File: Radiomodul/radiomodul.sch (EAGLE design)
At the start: 29 parts, among them IC1 MCP601R, Q1 12MHz, U1 LPC1343FBD48, U2 LM1117-3.3, U3 MCP130T

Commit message: the name corrected
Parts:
- removed D1: (no value), diode:DIODE-SMB
- removed D2: P6SMB18CA, Heinrich:SHOTKY-SMDSMB
- removed JP2: E31, microbuilder:HEADER-1X7ROUND
- removed R14, R16: 4k7, rcl:R-EU_R0805
- removed U3: MCP130T, microbuilder:MCP130TWAVE
- added C11, C12, C17: 100nF, rcl:C-EUC0805
- added C14: 100pF, rcl:C-EUC0805
- added C18: 10µF, Heinrich:CAP_TANTALUMSMCA
- added IC2: AD5243, Heinrich:AD5243
- added IC3: TXS0104, Heinrich:TXS0104
- added IC4: TXB0104PWR, Heinrich:TXB0104PWR
- added IC6: E910.15, Heinrich:E910.15
- added R5: 10, rcl:R-EU_R0805
- added R6: 10k, rcl:R-EU_R0805
- C7, C8: value 10uF -> 100nF; device rcl:CPOL-EUSMCC -> rcl:C-EUC0805
- U2: value LM1117-3.3 -> MCP130T; device microbuilder:LM1117SOT223-REFLOW -> microbuilder:MCP130TWAVE
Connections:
- removed net 12V: D1.A, JP2.1
- removed net G1: JP2.7
- removed net G2: JP2.6
- removed net G3: JP2.5
- removed net G4: JP2.4
- new net /SEN: IC4.A3, U1.PIO1_5/!RTS!/CT32B0_CAP0
- new net 5.0V: C10.1, C17.1, C18.+, C7.1, IC2.VDD, IC3.VCCB, IC4.VCCB, IC6.VCC
- new net IBUS: R5.2
- new net N$10: IC4.B3, IC6.SEN/STA
- new net N$7: IC4.B2, IC6.TXD
- new net N$9: C14.1, IC6.BUS, R5.1
- new net RING: IC3.A3, U1.PIO0_3/USB_VBUS
- new net RXD: IC4.A1, U1.PIO1_6/RXD/CT32B0_MAT0
- new net R_BASE: IC2.W2
- new net R_RING: IC3.B3
- new net R_TIP: IC2.A1
- new net TXD: IC4.A2, U1.PIO1_7/TXD/CT32B0_MAT1
- net /RESET: now also R6.1, U2.RST; no longer U3.RST
- net 3.3V: now also C11.1, C12.1, C8.1, IC3.OE, IC3.VCCA, IC4.OE, IC4.VCCA, R6.2, U2.VCC; no longer C10.1, C7.+, R14.2, R16.2, U2.OUT, U3.VCC
- net GND: now also C11.2, C12.2, C14.2, C17.2, C18.-, C7.2, C8.2, IC2.GND, IC3.GND, IC6.GND, U2.GND; no longer C7.-, C8.-, D2.A, JP2.2, U2.ADJ, U3.GND
- net LICHT: no longer JP2.3
- net N$1: now also IC2.SDA, IC3.B1; no longer C8.+, D1.C, D2.C, U2.IN
- net N$3: now also IC2.SCL, IC3.B2; no longer U1.PIO1_6/RXD/CT32B0_MAT0
- net N$5: now also IC4.B1, IC6.RXD; no longer U1.PIO1_7/TXD/CT32B0_MAT1
- net N$6: now also IC2.A2, IC2.W1; no longer U1.PIO1_5/!RTS!/CT32B0_CAP0
- net SCL: now also IC3.A2; no longer R16.1
- net SDA: now also IC3.A1; no longer R14.1

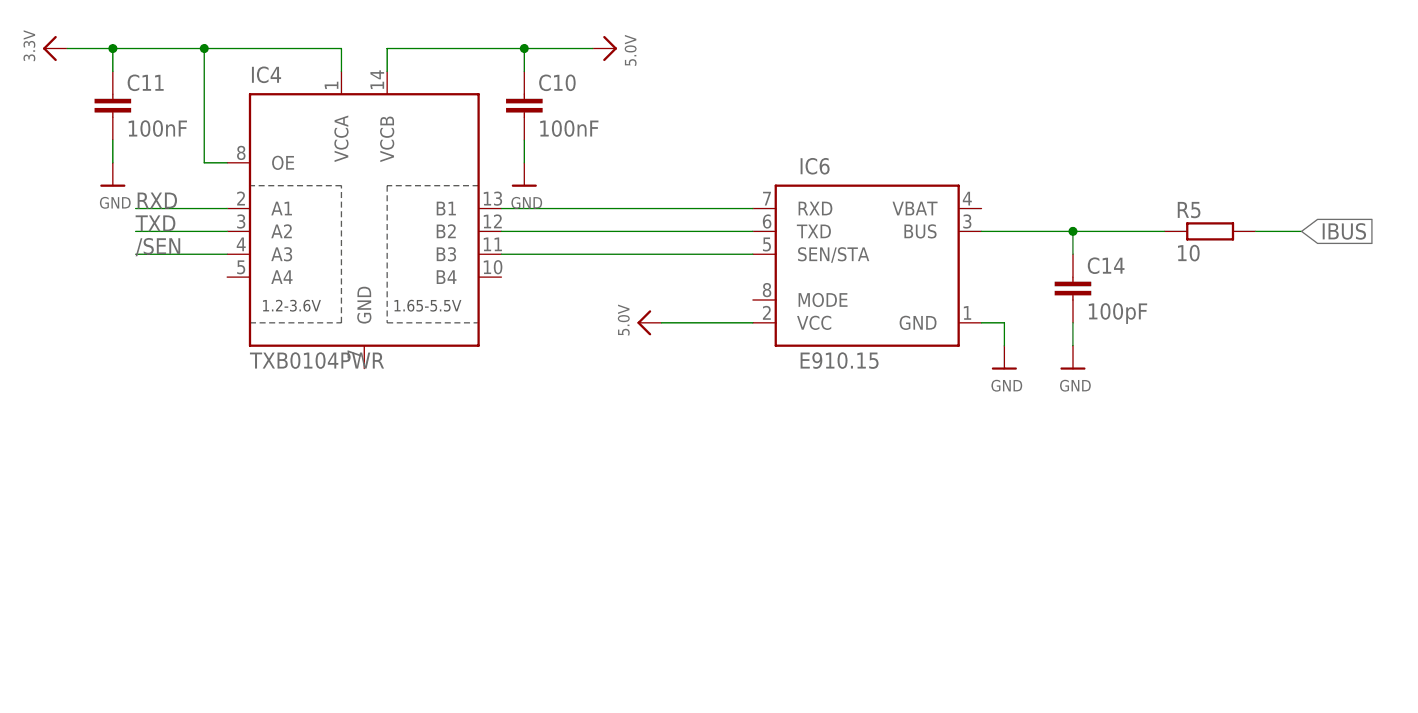
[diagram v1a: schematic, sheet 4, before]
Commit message: 
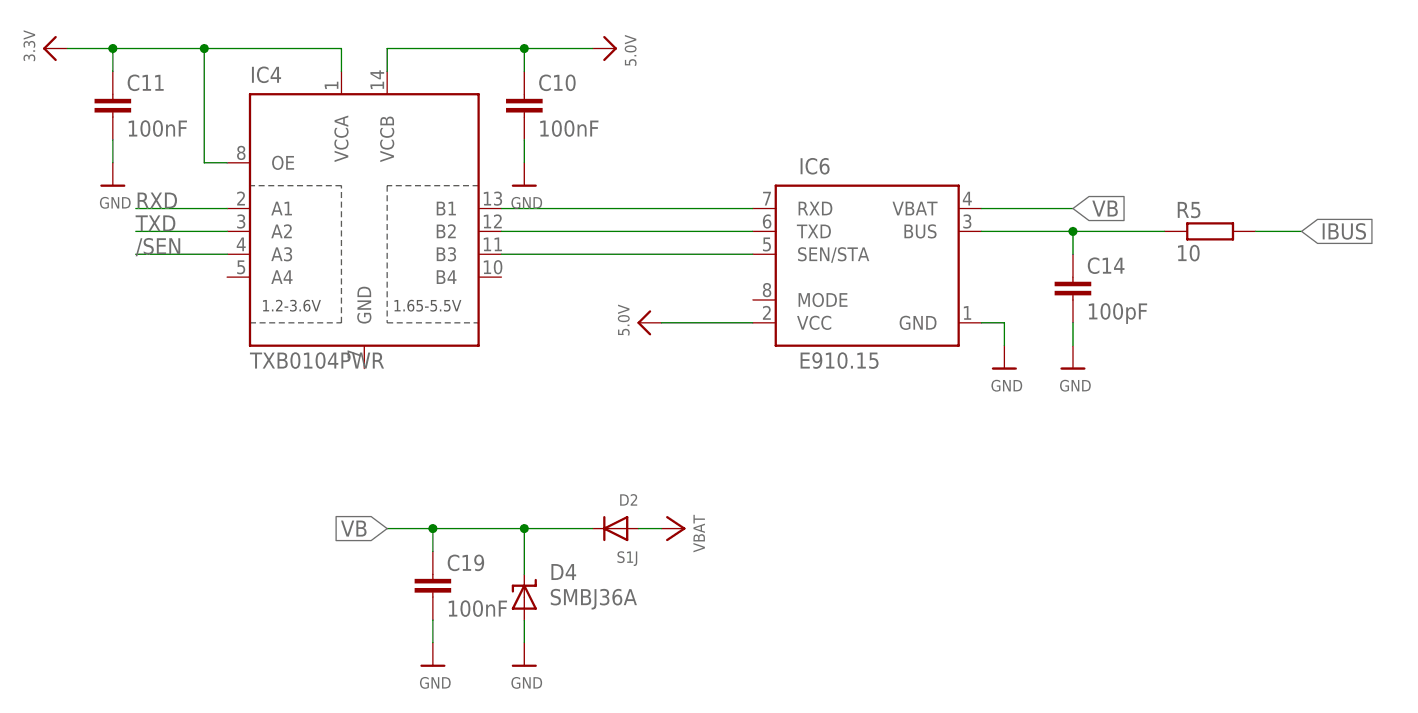
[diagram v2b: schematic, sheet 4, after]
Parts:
- added C13, C15, C19: 100nF, rcl:C-EUC0805
- added C16: 10µF/50V, rcl:CPOL-EUD
- added D1: SMBJ36CA, Heinrich:P6SMBXXCA
- added D2: S1J, Heinrich:DIODESMA
- added D4: SMBJ36A, diode:SUPPRESSOR-SMBJ
- added IC5, IC7: NCV4274CSOT-223, Heinrich:NCV4274CSOT-223
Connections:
- new net N$11: IC7.OUT
- new net N$12: IC5.OUT
- new net UBAT: C16.+, D1.2
- new net VB: C19.1, D2.C, D4.C, IC6.VBAT
- new net VBAT: C13.1, C15.1, D2.A, IC5.IN, IC7.IN
- net GND: now also C13.2, C15.2, C16.-, C19.2, D1.1, D4.A, IC5.GND, IC7.GND
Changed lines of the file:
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@@
 <part name="U$32" library="microbuilder" deviceset="GND" device=""/>
 <part name="R6" library="rcl" library_urn="urn:adsk.eagle:library:334" deviceset="R-EU_" device="R0805" package3d_urn="urn:adsk.eagle:package:23553/2" value="10k"/>
+<part name="IC5" library="Heinrich" deviceset="NCV4274C" device="SOT-223"/>
+<part name="IC7" library="Heinrich" deviceset="NCV4274C" device="SOT-223"/>
+<part name="U$33" library="microbuilder" deviceset="GND" device=""/>
+<part name="U$34" library="microbuilder" deviceset="GND" device=""/>
+<part name="C13" library="rcl" library_urn="urn:adsk.eagle:library:334" deviceset="C-EU" device="C0805" package3d_urn="urn:adsk.eagle:package:23617/2" value="100nF"/>
+<part name="C15" library="rcl" library_urn="urn:adsk.eagle:library:334" deviceset="C-EU" device="C0805" package3d_urn="urn:adsk.eagle:package:23617/2" value="100nF"/>
+<part name="U$38" library="microbuilder" deviceset="GND" device=""/>
+<part name="U$41" library="microbuilder" deviceset="GND" device=""/>
+<part name="D1" library="Heinrich" deviceset="P6SMBXXCA" device="" value="SMBJ36CA"/>
+<part name="U$42" library="microbuilder" deviceset="GND" device=""/>
+<part name="U$43" library="microbuilder" deviceset="VBAT" device=""/>
+<part name="U$44" library="microbuilder" deviceset="VBAT" device=""/>
+<part name="U$45" library="microbuilder" deviceset="VBAT" device=""/>
+<part name="C16" library="rcl" library_urn="urn:adsk.eagle:library:334" deviceset="CPOL-EU" device="D" package3d_urn="urn:adsk.eagle:package:23424/2" value="10µF/50V"/>
+<part name="U$46" library="microbuilder" deviceset="GND" device=""/>
+<part name="D2" library="Heinrich" deviceset="DIODE" device="SMA" value="S1J"/>
+<part name="U$47" library="microbuilder" deviceset="GND" device=""/>
+<part name="D4" library="diode" library_urn="urn:adsk.eagle:library:210" deviceset="SUPPRESSOR-" device="SMBJ" package3d_urn="urn:adsk.eagle:package:43442/2" value="SMBJ36A"/>
+<part name="C19" library="rcl" library_urn="urn:adsk.eagle:library:334" deviceset="C-EU" device="C0805" package3d_urn="urn:adsk.eagle:package:23617/2" value="100nF"/>
+<part name="U$48" library="microbuilder" deviceset="GND" device=""/>
+<part name="U$49" library="microbuilder" deviceset="VBAT" device=""/>
 </parts>
 <sheets>
@@
 <instances>
 <instance part="FRAME2" gate="G$1" x="0" y="0"/>
+<instance part="IC5" gate="G$1" x="93.98" y="111.76"/>
+<instance part="IC7" gate="G$1" x="93.98" y="86.36"/>
+<instance part="U$33" gate="G$1" x="106.68" y="78.74"/>
+<instance part="U$34" gate="G$1" x="106.68" y="104.14"/>
+<instance part="C13" gate="G$1" x="76.2" y="109.22"/>
+<instance part="C15" gate="G$1" x="76.2" y="83.82"/>
+<instance part="U$38" gate="G$1" x="76.2" y="99.06"/>
+<instance part="U$41" gate="G$1" x="76.2" y="73.66"/>
+<instance part="D1" gate="G$1" x="27.94" y="101.6" rot="R90"/>
+<instance part="U$42" gate="G$1" x="27.94" y="93.98"/>
+<instance part="U$43" gate="G$1" x="45.72" y="109.22" rot="R270"/>
+<instance part="U$44" gate="G$1" x="68.58" y="114.3" rot="R90"/>
+<instance part="U$45" gate="G$1" x="68.58" y="88.9" rot="R90"/>
+<instance part="C16" gate="G$1" x="40.64" y="104.14"/>
+<instance part="U$46" gate="G$1" x="40.64" y="93.98"/>
 </instances>
 <busses>
 </busses>
 <nets>
+<net name="GND" class="0">
+<segment>
+<pinref part="IC5" gate="G$1" pin="GND"/>
+<pinref part="U$34" gate="G$1" pin="GND"/>
+<wire x1="104.14" y1="109.22" x2="106.68" y2="109.22" width="0.1524" layer="91"/>
+<wire x1="106.68" y1="109.22" x2="106.68" y2="106.68" width="0.1524" layer="91"/>
+</segment>
+<segment>
+<pinref part="IC7" gate="G$1" pin="GND"/>
+<pinref part="U$33" gate="G$1" pin="GND"/>
+<wire x1="104.14" y1="83.82" x2="106.68" y2="83.82" width="0.1524" layer="91"/>
+<wire x1="106.68" y1="83.82" x2="106.68" y2="81.28" width="0.1524" layer="91"/>
+</segment>
+<segment>
+<pinref part="C13" gate="G$1" pin="2"/>
+<wire x1="76.2" y1="104.14" x2="76.2" y2="101.6" width="0.1524" layer="91"/>
+<pinref part="U$38" gate="G$1" pin="GND"/>
+</segment>
+<segment>
+<pinref part="C15" gate="G$1" pin="2"/>
+<wire x1="76.2" y1="78.74" x2="76.2" y2="76.2" width="0.1524" layer="91"/>
+<pinref part="U$41" gate="G$1" pin="GND"/>
+</segment>
+<segment>
+<pinref part="D1" gate="G$1" pin="1"/>
+<wire x1="27.94" y1="99.06" x2="27.94" y2="96.52" width="0.1524" layer="91"/>
+<pinref part="U$42" gate="G$1" pin="GND"/>
+</segment>
+<segment>
+<pinref part="C16" gate="G$1" pin="-"/>
+<wire x1="40.64" y1="99.06" x2="40.64" y2="96.52" width="0.1524" layer="91"/>
+<pinref part="U$46" gate="G$1" pin="GND"/>
+</segment>
+</net>
+<net name="N$11" class="0">
+<segment>
+<pinref part="IC7" gate="G$1" pin="OUT"/>
+<wire x1="104.14" y1="88.9" x2="124.46" y2="88.9" width="0.1524" layer="91"/>
+</segment>
+</net>
+<net name="N$12" class="0">
+<segment>
+<pinref part="IC5" gate="G$1" pin="OUT"/>
+<wire x1="104.14" y1="114.3" x2="124.46" y2="114.3" width="0.1524" layer="91"/>
+</segment>
+</net>
+<net name="VBAT" class="0">
+<segment>
+<pinref part="IC5" gate="G$1" pin="IN"/>
+<wire x1="83.82" y1="114.3" x2="76.2" y2="114.3" width="0.1524" layer="91"/>
+<pinref part="C13" gate="G$1" pin="1"/>
+<wire x1="76.2" y1="114.3" x2="68.58" y2="114.3" width="0.1524" layer="91"/>
+<wire x1="76.2" y1="111.76" x2="76.2" y2="114.3" width="0.1524" layer="91"/>
+<junction x="76.2" y="114.3"/>
+<pinref part="U$44" gate="G$1" pin="VBAT"/>
+</segment>
+<segment>
+<pinref part="IC7" gate="G$1" pin="IN"/>
+<wire x1="83.82" y1="88.9" x2="76.2" y2="88.9" width="0.1524" layer="91"/>
+<pinref part="C15" gate="G$1" pin="1"/>
+<wire x1="76.2" y1="88.9" x2="68.58" y2="88.9" width="0.1524" layer="91"/>
+<wire x1="76.2" y1="88.9" x2="76.2" y2="86.36" width="0.1524" layer="91"/>
+<junction x="76.2" y="88.9"/>
+<pinref part="U$45" gate="G$1" pin="VBAT"/>
+</segment>
+</net>
+<net name="UBAT" class="0">
+<segment>
+<label x="15.24" y="109.22" size="1.778" layer="95" rot="R180" xref="yes"/>
+<wire x1="15.24" y1="109.22" x2="27.94" y2="109.22" width="0.1524" layer="91"/>
+<pinref part="D1" gate="G$1" pin="2"/>
+<wire x1="27.94" y1="109.22" x2="40.64" y2="109.22" width="0.1524" layer="91"/>
+<wire x1="40.64" y1="109.22" x2="45.72" y2="109.22" width="0.1524" layer="91"/>
+<wire x1="27.94" y1="106.68" x2="27.94" y2="109.22" width="0.1524" layer="91"/>
+<junction x="27.94" y="109.22"/>
+<pinref part="U$43" gate="G$1" pin="VBAT"/>
+<pinref part="C16" gate="G$1" pin="+"/>
+<wire x1="40.64" y1="106.68" x2="40.64" y2="109.22" width="0.1524" layer="91"/>
+<junction x="40.64" y="109.22"/>
+</segment>
+</net>
 </nets>
 </sheet>
@@
 <instance part="U$25" gate="G$1" x="38.1" y="149.86" rot="R90"/>
 <instance part="U$26" gate="G$1" x="96.52" y="149.86" rot="R270"/>
+<instance part="D2" gate="G$1" x="99.06" y="96.52" rot="MR0"/>
+<instance part="U$47" gate="G$1" x="88.9" y="81.28"/>
+<instance part="D4" gate="G$1" x="88.9" y="88.9"/>
+<instance part="C19" gate="G$1" x="78.74" y="91.44"/>
+<instance part="U$48" gate="G$1" x="78.74" y="81.28"/>
+<instance part="U$49" gate="G$1" x="104.14" y="96.52" rot="R270"/>
 </instances>
 <busses>
@@
 <pinref part="U$13" gate="G$1" pin="GND"/>
 <wire x1="88.9" y1="139.7" x2="88.9" y2="137.16" width="0.1524" layer="91"/>
+</segment>
+<segment>
+<wire x1="88.9" y1="86.36" x2="88.9" y2="83.82" width="0.1524" layer="91"/>
+<pinref part="U$47" gate="G$1" pin="GND"/>
+<pinref part="D4" gate="G$1" pin="A"/>
+</segment>
+<segment>
+<pinref part="C19" gate="G$1" pin="2"/>
+<wire x1="78.74" y1="86.36" x2="78.74" y2="83.82" width="0.1524" layer="91"/>
+<pinref part="U$48" gate="G$1" pin="GND"/>
 </segment>
 </net>
@@
 </segment>
 </net>
+<net name="VB" class="0">
+<segment>
+<pinref part="IC6" gate="G$1" pin="VBAT"/>
+<wire x1="139.7" y1="132.08" x2="149.86" y2="132.08" width="0.1524" layer="91"/>
+<label x="149.86" y="132.08" size="1.778" layer="95" xref="yes"/>
+</segment>
+<segment>
+<pinref part="D2" gate="G$1" pin="C"/>
+<wire x1="96.52" y1="96.52" x2="88.9" y2="96.52" width="0.1524" layer="91"/>
+<wire x1="88.9" y1="96.52" x2="78.74" y2="96.52" width="0.1524" layer="91"/>
+<wire x1="78.74" y1="96.52" x2="73.66" y2="96.52" width="0.1524" layer="91"/>
+<wire x1="88.9" y1="91.44" x2="88.9" y2="96.52" width="0.1524" layer="91"/>
+<junction x="88.9" y="96.52"/>
+<pinref part="D4" gate="G$1" pin="C"/>
+<label x="73.66" y="96.52" size="1.778" layer="95" rot="R180" xref="yes"/>
+<pinref part="C19" gate="G$1" pin="1"/>
+<wire x1="78.74" y1="93.98" x2="78.74" y2="96.52" width="0.1524" layer="91"/>
+<junction x="78.74" y="96.52"/>
+</segment>
+</net>
+<net name="VBAT" class="0">
+<segment>
+<pinref part="D2" gate="G$1" pin="A"/>
+<wire x1="101.6" y1="96.52" x2="104.14" y2="96.52" width="0.1524" layer="91"/>
+<pinref part="U$49" gate="G$1" pin="VBAT"/>
+</segment>
+</net>
